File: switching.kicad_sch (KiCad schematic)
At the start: 16 parts, among them K1 SANYOU_SRD_Form_C, K2 SANYOU_SRD_Form_C, Q2 S8050_SMD, Q3 S8050_SMD

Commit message: Added footprints for HX711 circuit on PCB and modified pin assignment
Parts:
- Q2, Q3: footprint Package_TO_SOT_THT:TO-92_Inline -> Package_TO_SOT_SMD:SOT-23
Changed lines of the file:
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@@
       (effects (font (size 1.27 1.27)) (justify left))
     )
-    (property "Footprint" "Package_TO_SOT_THT:TO-92_Inline" (at 204.47 122.555 0)
+    (property "Footprint" "Package_TO_SOT_SMD:SOT-23" (at 204.47 122.555 0)
       (effects (font (size 1.27 1.27) italic) (justify left) hide)
     )
@@
       (effects (font (size 1.27 1.27)) (justify left))
     )
-    (property "Footprint" "Package_TO_SOT_THT:TO-92_Inline" (at 204.47 85.725 0)
+    (property "Footprint" "Package_TO_SOT_SMD:SOT-23" (at 204.47 85.725 0)
       (effects (font (size 1.27 1.27) italic) (justify left) hide)
     )

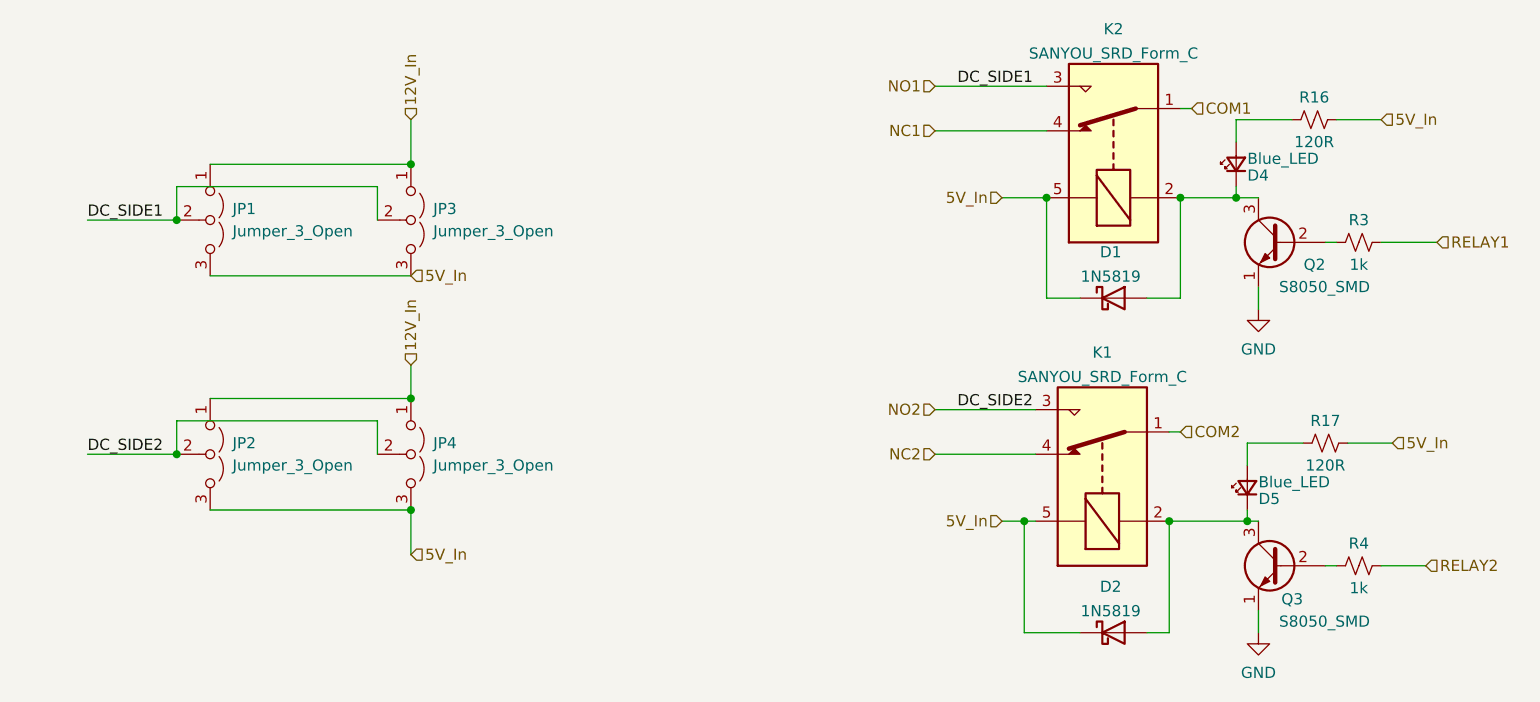
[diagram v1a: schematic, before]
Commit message: Fixed clearance violations and via sizing violations on pcb. Omitted 'mask aperture bridges' errors for jumpers.
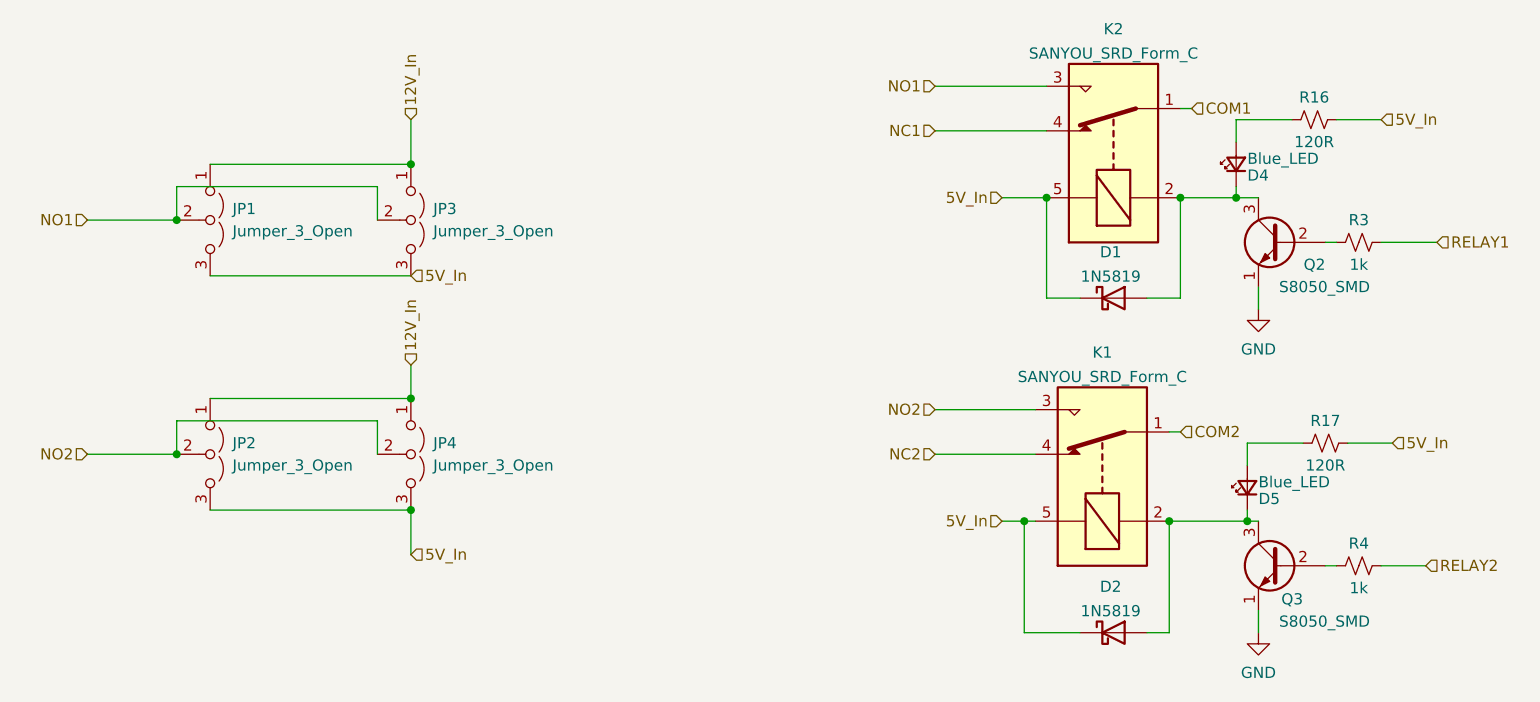
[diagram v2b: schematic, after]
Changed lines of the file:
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@@
     (stroke (width 0) (type default))
-  )
-  (label "DC_SIDE2" (at 73.66 107.95 0) (fields_autoplaced)
-    (effects (font (size 1.27 1.27)) (justify left bottom))
-  )
-  (label "DC_SIDE2" (at 172.72 102.87 0) (fields_autoplaced)
-    (effects (font (size 1.27 1.27)) (justify left bottom))
-  )
-  (label "DC_SIDE1" (at 172.72 66.04 0) (fields_autoplaced)
-    (effects (font (size 1.27 1.27)) (justify left bottom))
-  )
-  (label "DC_SIDE1" (at 73.66 81.28 0) (fields_autoplaced)
-    (effects (font (size 1.27 1.27)) (justify left bottom))
   )
   (hierarchical_label "NO2" (shape input) (at 170.18 102.87 180) (fields_autoplaced)
@@
   (hierarchical_label "COM2" (shape input) (at 198.12 105.41 0) (fields_autoplaced)
     (effects (font (size 1.27 1.27)) (justify left))
+  )
+  (hierarchical_label "NO2" (shape input) (at 73.66 107.95 180) (fields_autoplaced)
+    (effects (font (size 1.27 1.27)) (justify right))
   )
   (hierarchical_label "RELAY1" (shape input) (at 227.33 83.82 0) (fields_autoplaced)
@@
     (effects (font (size 1.27 1.27)) (justify right))
   )
+  (hierarchical_label "NO1" (shape input) (at 73.66 81.28 180) (fields_autoplaced)
+    (effects (font (size 1.27 1.27)) (justify right))
+  )

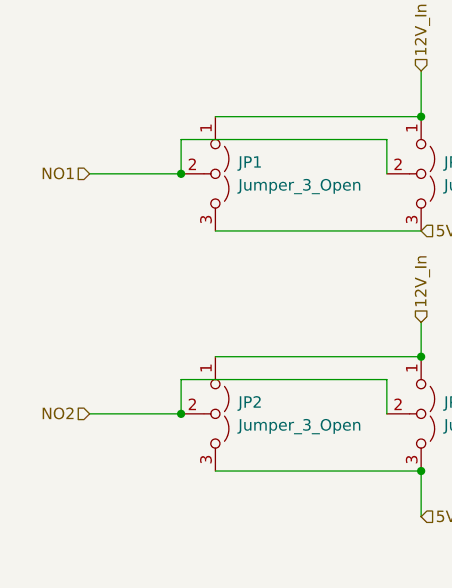
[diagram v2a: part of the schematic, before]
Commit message: Connected power to relay COMs
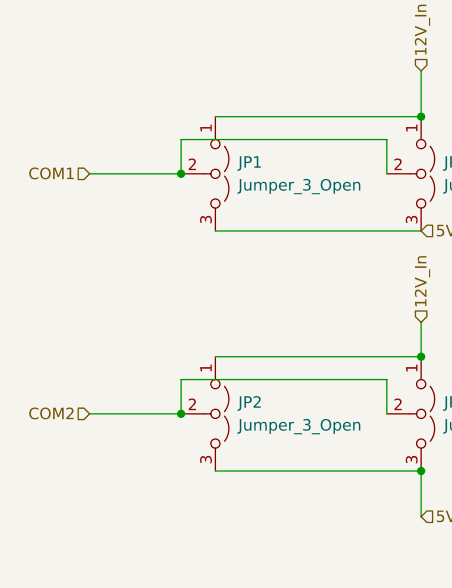
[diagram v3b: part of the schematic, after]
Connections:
- net COM1: now also JP1.2 (C), JP3.2 (C)
- net COM2: now also JP2.2 (C), JP4.2 (C)
- net NO1: no longer JP1.2 (C), JP3.2 (C)
- net NO2: no longer JP2.2 (C), JP4.2 (C)
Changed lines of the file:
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@@
     (effects (font (size 1.27 1.27)) (justify left))
-  )
-  (hierarchical_label "NO2" (shape input) (at 73.66 107.95 180) (fields_autoplaced)
-    (effects (font (size 1.27 1.27)) (justify right))
   )
   (hierarchical_label "RELAY1" (shape input) (at 227.33 83.82 0) (fields_autoplaced)
@@
     (effects (font (size 1.27 1.27)) (justify right))
   )
+  (hierarchical_label "COM1" (shape input) (at 73.66 81.28 180) (fields_autoplaced)
+    (effects (font (size 1.27 1.27)) (justify right))
+  )
+  (hierarchical_label "COM2" (shape input) (at 73.66 107.95 180) (fields_autoplaced)
+    (effects (font (size 1.27 1.27)) (justify right))
+  )
   (hierarchical_label "NC1" (shape input) (at 170.18 71.12 180) (fields_autoplaced)
     (effects (font (size 1.27 1.27)) (justify right))
@@
     (effects (font (size 1.27 1.27)) (justify right))
   )
-  (hierarchical_label "NO1" (shape input) (at 73.66 81.28 180) (fields_autoplaced)
-    (effects (font (size 1.27 1.27)) (justify right))
-  )
